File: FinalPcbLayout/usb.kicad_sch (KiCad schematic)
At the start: 26 parts, among them J5 USB_C_Receptacle, Q2 S8050, Q3 S8050, U7 93LCxxB, Y1 12Mhz

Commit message: More Schematic Label Updates
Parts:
- U6: value ~ -> FT232HPQ
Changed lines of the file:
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@@
       (effects (font (size 1.27 1.27)))
     )
-    (property "Value" "~" (at 107.95 140.97 0)
+    (property "Value" "FT232HPQ" (at 107.95 140.97 0)
       (effects (font (size 1.27 1.27)))
     )

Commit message: Updated CSV
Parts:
- C20: digikey_pn (none) -> 445-7476-1-ND
- C21, C22: digikey_pn (none) -> 1292-1494-1-ND
- C23: digikey_pn (none) -> 1276-2041-1-ND
- C24: value .1u -> 0.1uF; digikey_pn (none) -> 1276-1935-1-ND
- J5: digikey_pn (none) -> WM12856CT-ND
- Q2, Q3: digikey_pn (none) -> 4878-BC547BBK-ND
- R14, R15: digikey_pn (none) -> RMCF0603FT10K0CT-ND
- R16, R17: digikey_pn (none) -> RMCF0603FT1K00CT-ND
- R18: digikey_pn (none) -> 13-RP0603BRD0725RLCT-ND
- R19: digikey_pn (none) -> 1292-WR06X680JTLCT-ND
- R20: digikey_pn (none) -> RMCF0603FT100KCT-ND
- R21: digikey_pn (none) -> P15KDBCT-ND
- R22: digikey_pn (none) -> P2.00KHCT-ND
- R26, R27, R28: value 10k -> 10k 1%; digikey_pn (none) -> RMCF0603FT10K0CT-ND
- R9: digikey_pn (none) -> RMCF0603FT12K0CT-ND
- U6: digikey_pn (none) -> 768-FT232HPQ-TRAY-ND
- Y1: digikey_pn (none) -> 3155-OSC12M-3.3I/S3TCT-ND
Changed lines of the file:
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@@
+      (effects (font (size 1.27 1.27)) hide)
+    )
+    (property "digikey_pn" "1292-1494-1-ND" (at 48.26 127 0)
       (effects (font (size 1.27 1.27)) hide)
     )
@@
       (effects (font (size 1.27 1.27)) (justify left) hide)
     )
+    (property "digikey_pn" "4878-BC547BBK-ND " (at 238.76 142.24 0)
+      (effects (font (size 1.27 1.27)) hide)
+    )
     (pin "1")
     (pin "2")
@@
       (effects (font (size 1.27 1.27)))
     )
-    (property "Value" "10k" (at 74.93 102.87 90)
+    (property "Value" "10k 1%" (at 74.93 102.87 90)
       (effects (font (size 1.27 1.27)))
     )
@@
       (effects (font (size 1.27 1.27)) hide)
     )
+    (property "digikey_pn" "RMCF0603FT10K0CT-ND" (at 74.93 105.41 0)
+      (effects (font (size 1.27 1.27)) hide)
+    )
     (pin "1")
     (pin "2")
@@
       (effects (font (size 1.27 1.27)))
     )
-    (property "Value" "10k" (at 59.69 107.95 90)
+    (property "Value" "10k 1%" (at 59.69 107.95 90)
       (effects (font (size 1.27 1.27)))
     )
@@
     )
     (property "Sim.Enable" "0" (at 59.69 110.49 0)
+      (effects (font (size 1.27 1.27)) hide)
+    )
+    (property "digikey_pn" "RMCF0603FT10K0CT-ND" (at 59.69 110.49 0)
       (effects (font (size 1.27 1.27)) hide)
     )
@@
       (effects (font (size 1.27 1.27)) (justify left) hide)
     )
+    (property "digikey_pn" "4878-BC547BBK-ND " (at 238.76 116.84 0)
+      (effects (font (size 1.27 1.27)) hide)
+    )
     (pin "1")
     (pin "2")
@@
       (effects (font (size 1.27 1.27)) hide)
     )
+    (property "digikey_pn" "1276-2041-1-ND" (at 95.25 35.56 0)
+      (effects (font (size 1.27 1.27)) hide)
+    )
     (pin "1")
     (pin "2")
@@
     )
     (property "Sim.Enable" "0" (at 48.26 137.16 0)
+      (effects (font (size 1.27 1.27)) hide)
+    )
+    (property "digikey_pn" "1292-1494-1-ND" (at 48.26 137.16 0)
       (effects (font (size 1.27 1.27)) hide)
     )
@@
       (effects (font (size 1.27 1.27)) hide)
     )
+    (property "digikey_pn" "RMCF0603FT1K00CT-ND" (at 139.7 177.8 0)
+      (effects (font (size 1.27 1.27)) hide)
+    )
     (pin "1")
     (pin "2")
@@
       (effects (font (size 1.27 1.27)) hide)
     )
+    (property "digikey_pn" "P15KDBCT-ND" (at 83.82 35.56 0)
+      (effects (font (size 1.27 1.27)) hide)
+    )
     (pin "1")
     (pin "2")
@@
       (effects (font (size 1.27 1.27)) hide)
     )
+    (property "digikey_pn" "P2.00KHCT-ND" (at 254 45.72 0)
+      (effects (font (size 1.27 1.27)) hide)
+    )
     (pin "1")
     (pin "2")
@@
     )
     (property "Sim.Enable" "0" (at 149.86 132.08 0)
+      (effects (font (size 1.27 1.27)) hide)
+    )
+    (property "digikey_pn" "1292-WR06X680JTLCT-ND " (at 149.86 132.08 0)
       (effects (font (size 1.27 1.27)) hide)
     )
@@
     )
     (property "Sim.Enable" "0" (at 139.7 132.08 0)
+      (effects (font (size 1.27 1.27)) hide)
+    )
+    (property "digikey_pn" "13-RP0603BRD0725RLCT-ND" (at 139.7 132.08 0)
       (effects (font (size 1.27 1.27)) hide)
     )
@@
       (effects (font (size 1.27 1.27)))
     )
-    (property "Value" "10k" (at 67.31 105.41 90)
+    (property "Value" "10k 1%" (at 67.31 105.41 90)
       (effects (font (size 1.27 1.27)))
     )
@@
     )
     (property "Sim.Enable" "0" (at 67.31 107.95 0)
+      (effects (font (size 1.27 1.27)) hide)
+    )
+    (property "digikey_pn" "RMCF0603FT10K0CT-ND" (at 67.31 107.95 0)
       (effects (font (size 1.27 1.27)) hide)
     )
@@
       (effects (font (size 1.27 1.27)) hide)
     )
+    (property "digikey_pn" "445-7476-1-ND" (at 72.39 152.4 0)
+      (effects (font (size 1.27 1.27)) hide)
+    )
     (pin "1")
     (pin "2")
@@
       (effects (font (size 1.27 1.27)) hide)
     )
+    (property "digikey_pn" "RMCF0603FT10K0CT-ND" (at 226.06 116.84 0)
+      (effects (font (size 1.27 1.27)) hide)
+    )
     (pin "1")
     (pin "2")
@@
     )
     (property "Sim.Enable" "0" (at 226.06 142.24 0)
+      (effects (font (size 1.27 1.27)) hide)
+    )
+    (property "digikey_pn" "RMCF0603FT10K0CT-ND" (at 226.06 142.24 0)
       (effects (font (size 1.27 1.27)) hide)
     )
@@
     )
     (property "Sim.Enable" "0" (at 107.95 142.24 0)
+      (effects (font (size 1.27 1.27)) hide)
+    )
+    (property "digikey_pn" "768-FT232HPQ-TRAY-ND " (at 107.95 142.24 0)
       (effects (font (size 1.27 1.27)) hide)
     )
@@
       (effects (font (size 1.27 1.27)) hide)
     )
+    (property "digikey_pn" "3155-OSC12M-3.3I/S3TCT-ND" (at 48.26 132.08 0)
+      (effects (font (size 1.27 1.27)) hide)
+    )
     (pin "1")
     (pin "2")
@@
     )
     (property "Sim.Enable" "0" (at 35.56 46.99 0)
+      (effects (font (size 1.27 1.27)) hide)
+    )
+    (property "digikey_pn" "WM12856CT-ND" (at 35.56 46.99 0)
       (effects (font (size 1.27 1.27)) hide)
     )
@@
       (effects (font (size 1.27 1.27)) hide)
     )
+    (property "digikey_pn" "RMCF0603FT1K00CT-ND" (at 139.7 175.26 0)
+      (effects (font (size 1.27 1.27)) hide)
+    )
     (pin "1")
     (pin "2")
@@
       (effects (font (size 1.27 1.27)) hide)
     )
+    (property "digikey_pn" "RMCF0603FT100KCT-ND" (at 83.82 25.4 0)
+      (effects (font (size 1.27 1.27)) hide)
+    )
     (pin "1")
     (pin "2")
@@
       (effects (font (size 1.27 1.27)))
     )
-    (property "Value" ".1u" (at 227.3363 29.21 90)
+    (property "Value" "0.1uF" (at 227.3363 29.21 90)
       (effects (font (size 1.27 1.27)))
     )
@@
       (effects (font (size 1.27 1.27)) hide)
     )
+    (property "digikey_pn" "1276-1935-1-ND" (at 227.33 33.02 0)
+      (effects (font (size 1.27 1.27)) hide)
+    )
     (pin "1")
     (pin "2")
@@
       (effects (font (size 1.27 1.27)) hide)
     )
+    (property "digikey_pn" "RMCF0603FT12K0CT-ND" (at 66.04 128.27 0)
+      (effects (font (size 1.27 1.27)) hide)
+    )

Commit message: Generated Bill of Materials
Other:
- company: (none) -> Rose-Hulman Institute of Technology
- title: (none) -> USB C / USB PD Programming
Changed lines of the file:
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@@
 (kicad_sch (version 20230121) (generator eeschema)
   (paper "A4")
+  (title_block
+    (title "USB C / USB PD Programming")
+    (date "2024-02-11")
+    (rev "1.0")
+    (company "Rose-Hulman Institute of Technology")
+    (comment 1 "Author: Jake Armstrong")
+  )
   (junction (at 83.82 157.48) (diameter 0) (color 0 0 0 0)
   )

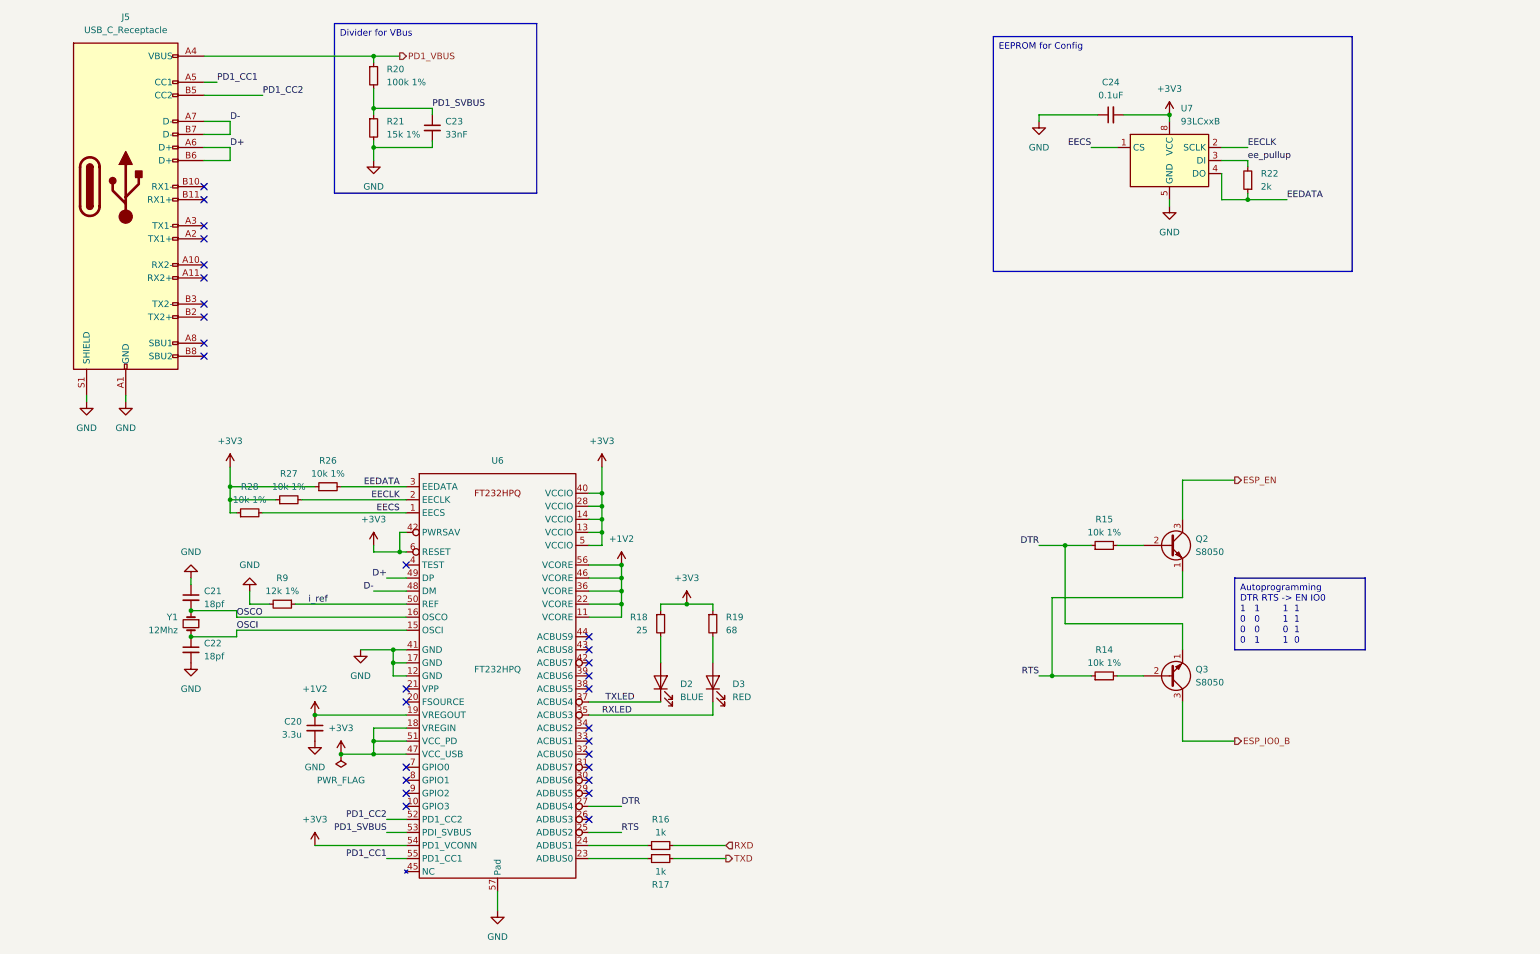
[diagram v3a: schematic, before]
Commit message: Axed Several Broken & Unused Parts
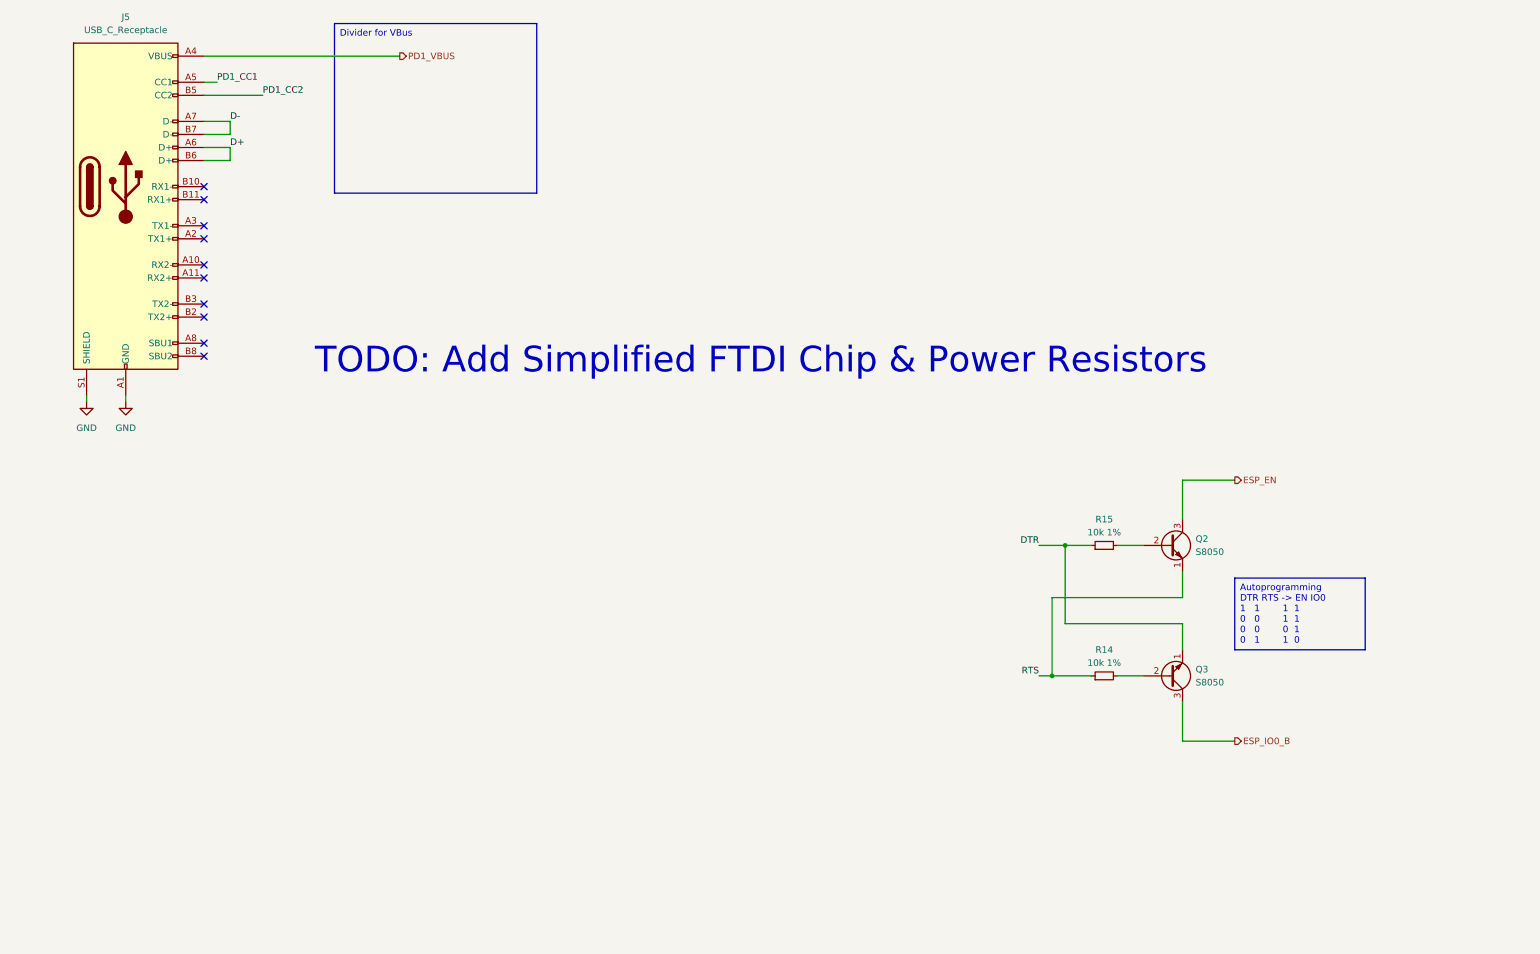
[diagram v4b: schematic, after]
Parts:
- removed C20: 3.3u, Capacitor_SMD:C_0603_1608Metric, symbol Device:C_Small
- removed C21, C22: 18pf, Capacitor_SMD:C_0603_1608Metric, symbol Device:C_Small
- removed C23: 33nF, Capacitor_SMD:C_0603_1608Metric, symbol Device:C_Small
- removed C24: 0.1uF, Capacitor_SMD:C_0603_1608Metric, symbol Device:C_Small
- removed D2: BLUE, LED_SMD:LED_0603_1608Metric, symbol Device:LED
- removed D3: RED, LED_SMD:LED_0603_1608Metric, symbol Device:LED
- removed R16, R17: 1k, Resistor_SMD:R_0603_1608Metric, symbol Device:R_Small
- removed R18: 25, Resistor_SMD:R_0603_1608Metric, symbol Device:R_Small
- removed R19: 68, Resistor_SMD:R_0603_1608Metric, symbol Device:R_Small
- removed R20: 100k 1%, Resistor_SMD:R_0603_1608Metric, symbol Device:R_Small
- removed R21: 15k 1%, Resistor_SMD:R_0603_1608Metric, symbol Device:R_Small
- removed R22: 2k, Resistor_SMD:R_0603_1608Metric, symbol Device:R_Small
- removed R26, R27, R28: 10k 1%, Resistor_SMD:R_0603_1608Metric, symbol Device:R_Small
- removed R9: 12k 1%, Resistor_SMD:R_0603_1608Metric, symbol Device:R_Small
- removed U6: FT232HPQ, Package_DFN_QFN:QFN-56-1EP_8x8mm_P0.5mm_EP4.5x5.2mm_ThermalVias, symbol OSMI-parts:FT232HPQ
- removed U7: 93LCxxB, Package_SO:SOIC-8_3.9x4.9mm_P1.27mm, symbol Memory_EEPROM:93LCxxB
- removed Y1: 12Mhz, Crystal:Crystal_SMD_SeikoEpson_FA238-4Pin_3.2x2.5mm, symbol Device:Crystal_Small
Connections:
- no-connect marks 29 -> 10
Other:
- note added: "TODO: Add Simplified FTDI Chip & Power Resistors"
